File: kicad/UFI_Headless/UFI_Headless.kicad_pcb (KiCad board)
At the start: 4 copper layers, 110 x 85 mm, 159 parts, among them J1 USB-C, J10 104031-0811, J11 WRITE_LOCK, J2 12V DC 5.5/2.1, J3 FDD_PWR, J4 SWD, J5 DBG_UART, J6 FDD_34PIN, J7 AMIGA_FDD, J8 IEC_HDR, J9 EXPANSION, Q1 AO3401A, Q2 2N7002, Q3 AO3401A, Q4 2N7002, SW1 RESET, SW2 BOOT, SW3 BTN_A, SW4 BTN_B, U1 USBLC6-2SC6, U10 74LVC14AD, U11 APS6404L-3SQR-SN, U12 INA180A1, U13 INA180A1, U14 74LVC1G32GW, U2 TPS54202DDC, U3 TPS2116DRL, U4 AP7361C-33E, U5 STM32H723ZGT6, U6 SN74LS07D, U7 SN74LS07D, U8 74LVC14AD, U9 SN74LS07D, Y1 25MHz CL=12pF

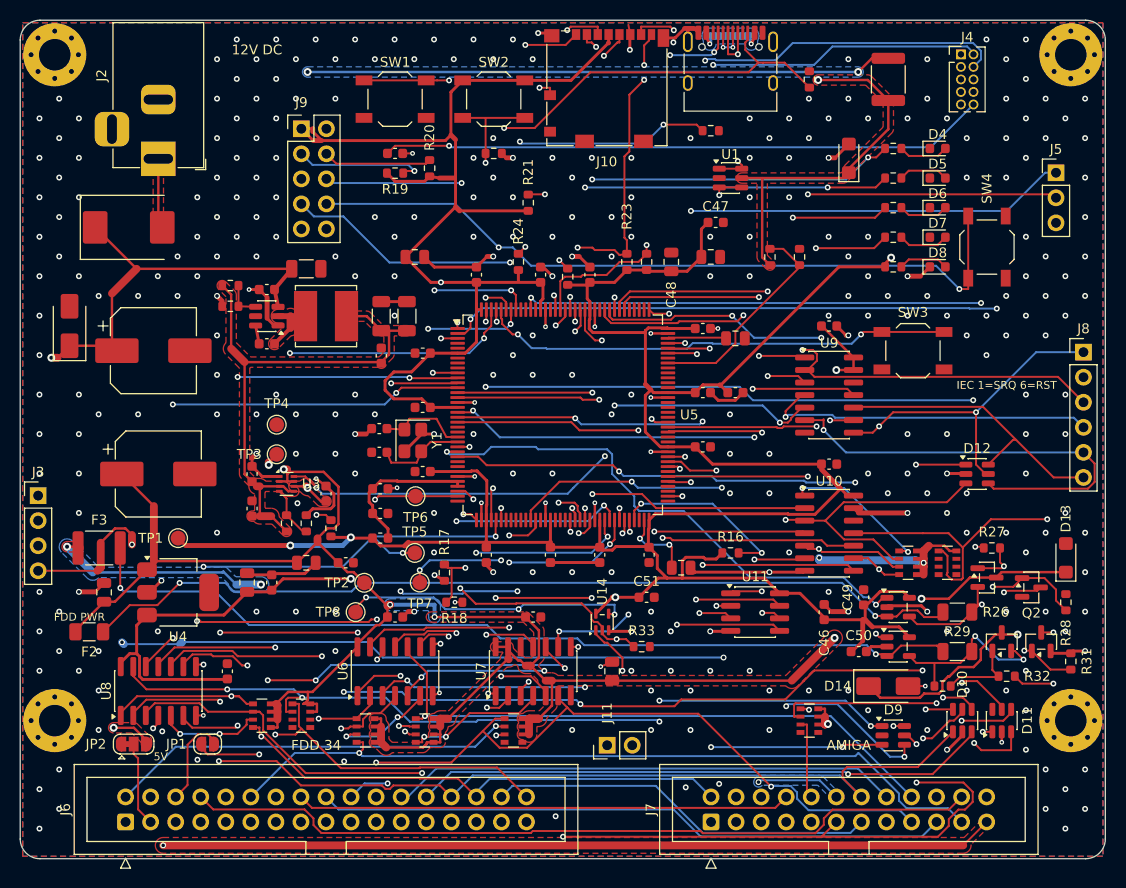
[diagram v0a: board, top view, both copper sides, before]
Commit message: v0.6: soldered SD NAND replaces the microSD slot; stand-alone dump + USB drive mode
Board (closed enclosure, no card access):
- J10 microSD removed; U15 SD NAND CSNP32GCR01-AOW (4 GB, C2841139) on the same
  SDMMC2 lines, project footprint fits MKDV8GIL-AST (1 GB) as well
- PG13 card detect dropped; board ID R18 4.7k (1055 mV = v0.6)
- project symbol/footprint library lib/, kisch.py + add_parts.py look there first
- ECO re-route; ERC 0, DRC 0 incl. warnings, 0 unconnected, parity clean, no via-in-pad
- new eco tools remove_part.py, set_value.py; fab outputs regenerated

Firmware 1.3:
- ufi_sd.c: block access + FatFs R0.12c disk glue (Cube middleware, ffconf.h)
- ufi_dump.c: button A >= 1 s / DUMP_START dumps the disk to DUMPnnnn.SCP,
  byte-identical to `ufi read-disk` (host simulation, 5 configurations);
  button B aborts, ERR blink codes
- USB mass storage mode (ST MSC class, ufi_msc.c): button B >= 2 s or USB_MSC
- commands 0x50-0x53, error code 13 (storage), GET_INFO knows v0.6
- CI: FatFs added to the sparse STM32CubeH7 checkout

Docs: READMEs, ordering guide (part cost, 1 GB alternative), bring-up checklist.
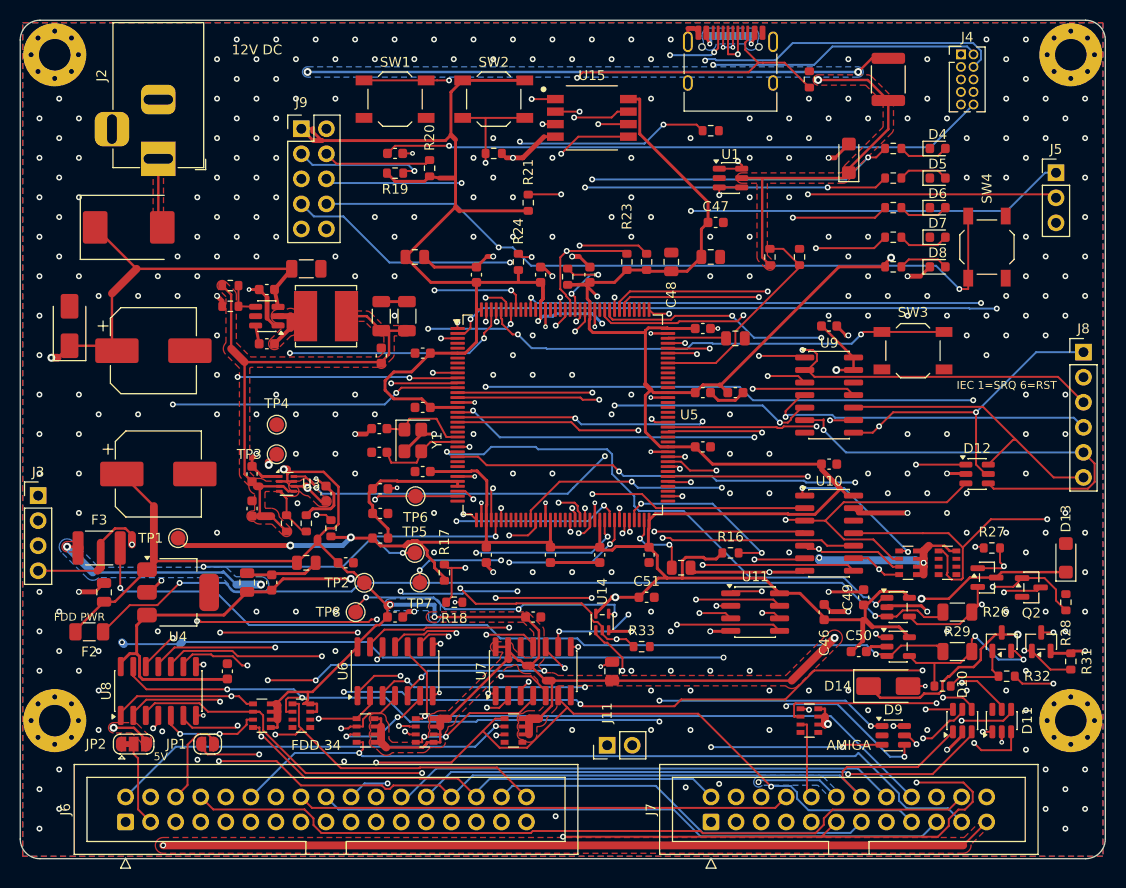
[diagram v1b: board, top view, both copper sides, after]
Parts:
- removed J10: 104031-0811, Connector_Card:microSD_HC_Molex_104031-0811
- added U15: CSNP32GCR01-AOW, UFI_Headless:SD_NAND_LGA-8_6x8mm_P1.27mm, F.Cu at (58.0, 9.90)
- R18: value 10k -> 4.7k
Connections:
- U5 pad 128: /MCU_Core/SD_CD -> unconnected-(U5-PG13-Pad128)
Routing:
- net +3V3: track 451.2 -> 480.0 mm, vias 7 -> 8
- net /MCU_Core/SD_CD: track 25.0 -> 0.00 mm, vias 2 -> 0
- net /MCU_Core/SD_D0: track 46.0 -> 26.9 mm
- net /MCU_Core/SD_CMD: track 40.9 -> 30.5 mm
- net /MCU_Core/SD_CLK: track 36.1 -> 26.3 mm
- net /MCU_Core/SD_D2: track 38.3 -> 29.9 mm
- net /MCU_Core/SD_D3: track 38.2 -> 33.8 mm, vias 2 -> 3
- net /MCU_Core/SD_D1: track 35.4 -> 32.4 mm, vias 4 -> 2
- net GND: track 146.9 -> 149.5 mm, vias 323 -> 325
- net FD_INDEX: track 122.0 -> 121.2 mm
- net CC2: track 80.8 -> 81.4 mm

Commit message: v0.6: front panel LED header J12 (2x4, one row per LED) with 330R R34-R37
Enclosure LEDs: 1+/2- PWR (3V3), 3+/4- ACT, 5+/6- FDD, 7+/8- ERR, parallel to the
board LEDs (~4 mA each), no firmware change. Placed top left (22, 9), ECO re-route;
resistor references hidden (new eco/hide_ref.py), '12V DC' label re-placed.
DRC 0 incl. warnings, 0 unconnected, parity clean, no via-in-pad; fab outputs,
README, ordering guide (J12 hand-sourced) and bring-up step 4.6a updated.
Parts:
- added J12: FRONT_LED, Connector_PinHeader_2.54mm:PinHeader_2x04_P2.54mm_Vertical, F.Cu at (21.0, 9.00)
- added R34: 330, Resistor_SMD:R_0603_1608Metric, F.Cu at (26.0, 4.50)
- added R35: 330, Resistor_SMD:R_0603_1608Metric, F.Cu at (28.0, 2.50)
- added R36: 330, Resistor_SMD:R_0603_1608Metric, F.Cu at (24.0, 5.00)
- added R37: 330, Resistor_SMD:R_0603_1608Metric, F.Cu at (30.0, 2.50)
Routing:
- net /MCU_Core/LED_ERR: track 40.7 -> 159.2 mm, vias 2 -> 4
- net /MCU_Core/LED_FDD: track 65.2 -> 109.1 mm, vias 3 -> 4
- net /MCU_Core/LED_ACT: track 69.0 -> 110.0 mm, vias 3 -> 4
- net /MCU_Core/FRONT_ERR: track 0.00 -> 21.3 mm, vias 0 -> 1
- net /MCU_Core/FRONT_ACT: track 0.00 -> 16.1 mm
- net /MCU_Core/FRONT_FDD: track 0.00 -> 12.6 mm, vias 0 -> 1
- net /MCU_Core/FRONT_PWR: track 0.00 -> 8.89 mm
- net +3V3: track 480.0 -> 486.7 mm
- net GND: vias 325 -> 308
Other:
- board text added: "FRONT LED"
